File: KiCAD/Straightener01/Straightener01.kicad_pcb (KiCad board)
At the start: 4 copper layers, 55.8 x 20 mm, 13 parts, among them IC1 LT3045EDD, J1 C112640, J2 C112640

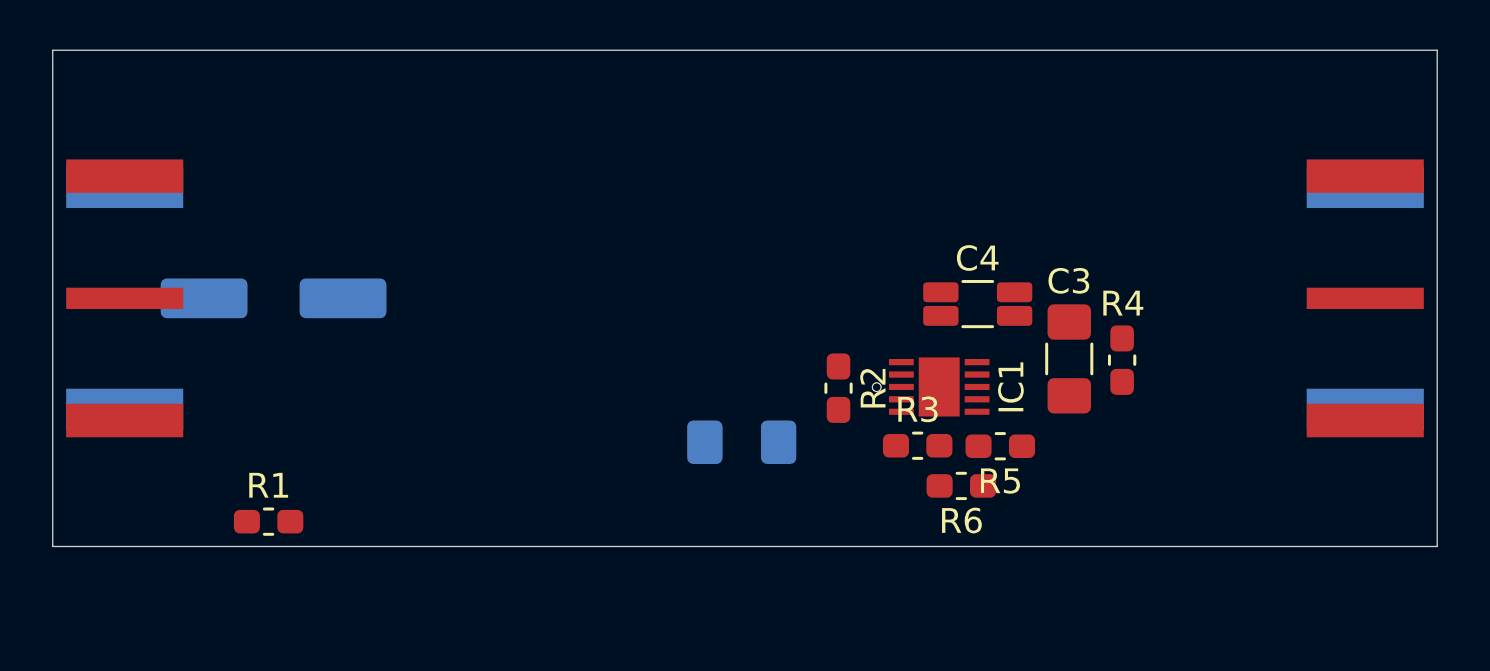
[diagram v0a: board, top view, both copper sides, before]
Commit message: more plane work on Straightener01
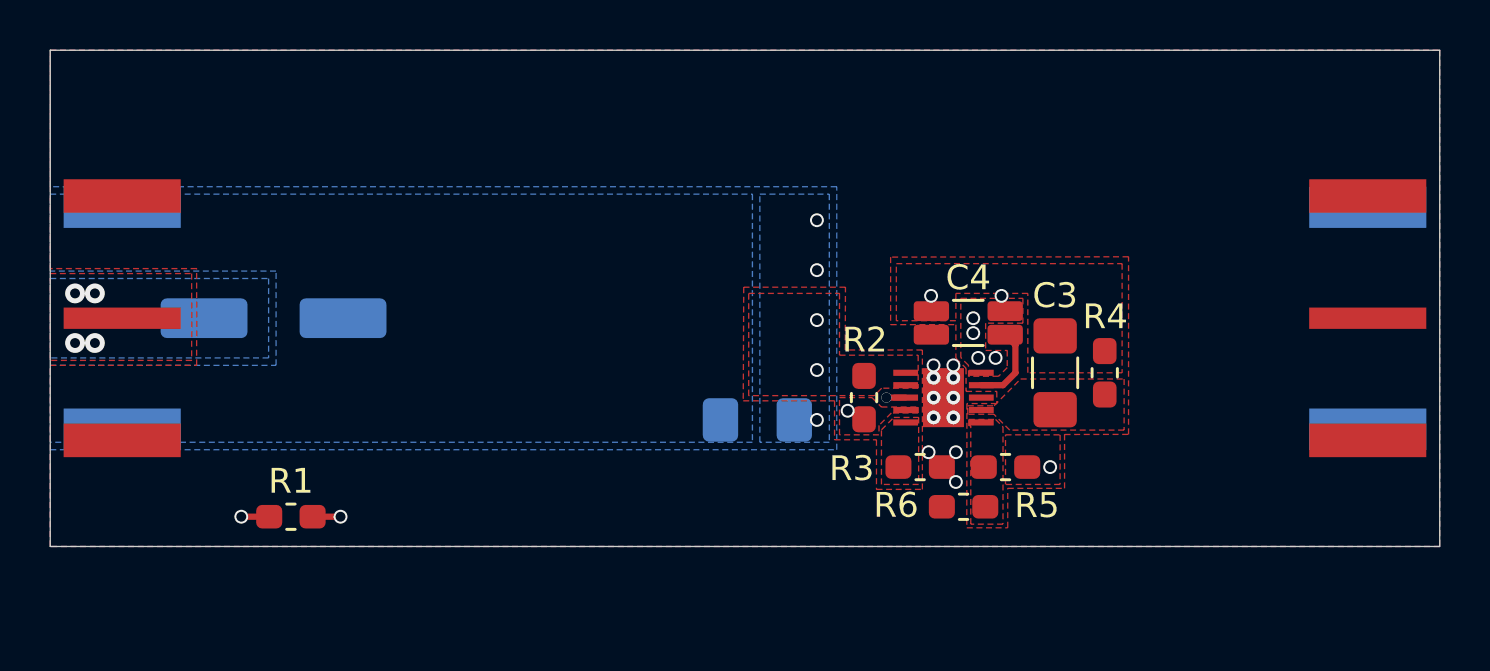
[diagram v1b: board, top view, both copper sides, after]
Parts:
- moved C2 1.10 mm to (125.5, 104.9)
- moved R2 1.10 mm to (129.8, 104.0)
- moved R1 0.92 mm to (106.7, 108.8)
- moved R4 0.87 mm to (139.5, 103.0)
- moved R5 0.87 mm to (135.5, 106.8)
- moved R3 0.87 mm to (132.1, 106.8)
- moved C4 0.85 mm to (134.0, 101.0)
- moved R6 0.84 mm to (133.8, 108.4)
- moved J1 0.81 mm to (99.9, 100.8)
- moved J2 0.81 mm to (150.1, 100.8)
- moved C1 0.80 mm to (106.0, 100.8)
- moved C3 0.80 mm to (137.5, 103.0)
- moved IC1 0.46 mm to (133.0, 104.0)
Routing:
- net /EN_UV: track 0.00 -> 27.0 mm, vias 1 -> 2
- net /VIN: track 0.00 -> 13.1 mm, vias 0 -> 10
- net /VOUT: track 0.00 -> 6.27 mm, vias 0 -> 6
- net /OUTS: track 0.00 -> 3.29 mm
- net Net-(C3-Pad2): vias 0 -> 1
- net GND: vias 0 -> 11
- net /PG: vias 0 -> 1
- added copper zone on F.Cu, net /ILIM
- added copper zone on F.Cu, net /PG
- added copper zone on F.Cu, net /PGFB
- added copper zone on F.Cu, net /SET
- added copper zone on B.Cu, net /VIN
- added copper zone on F.Cu, net /VIN
- added copper zone on In2.Cu, net /VIN
- added copper zone on F.Cu, net /VOUT
- added copper zone on In2.Cu, net /VOUT
- added copper zone on B.Cu, net GND
- added copper zone on F.Cu, net GND
- added copper zone on In1.Cu, net GND
- added copper zone on In2.Cu, net GND
- added copper zone on F.Cu, net Net-(C3-Pad2)
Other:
- board size 55.8 x 20 mm -> 56 x 20 mm

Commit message: finished up Straightener01
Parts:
- C1: footprint Capacitor_SMD:CP_Elec_6.3x5.4 -> Capacitor_SMD:CP_Elec_5x5.3
- moved J1 5.00 mm to (104.9, 100.8)
- moved R1 5.00 mm to (111.7, 108.8)
- moved C1 1.60 mm to (107.6, 100.8)
- moved C3 0.10 mm to (137.6, 103.0)
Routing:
- net GND: track 0.00 -> 5.71 mm, vias 11 -> 74
- net /EN_UV: track 27.0 -> 21.5 mm
- net /VOUT: track 6.27 -> 9.17 mm, vias 6 -> 7
- net /SET: track 0.00 -> 0.75 mm
- net /PG: track 0.00 -> 0.67 mm
- net /VIN: track 13.1 -> 13.6 mm
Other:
- board size 56 x 20 mm -> 51 x 20 mm
- board text added: "Dylan Oh"
- board text added: "Feb 2020"
- board text added: "Straightener01"
